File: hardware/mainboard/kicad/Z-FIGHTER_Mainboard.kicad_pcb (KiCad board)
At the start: 2 copper layers, 100 x 150 mm, 55 parts, among them IC1 Z80SIO, J1 DB9_Male_MountingHoles, J2 DB9_Male_MountingHoles, J3 USB_B, J4 Conn_02x13_Odd_Even, J5 Conn_Parallel_User, J6 Conn_PATA, J7 Conn_02x04_Odd_Even, SW1 SW_Push, SW2 SW_DIP_x03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

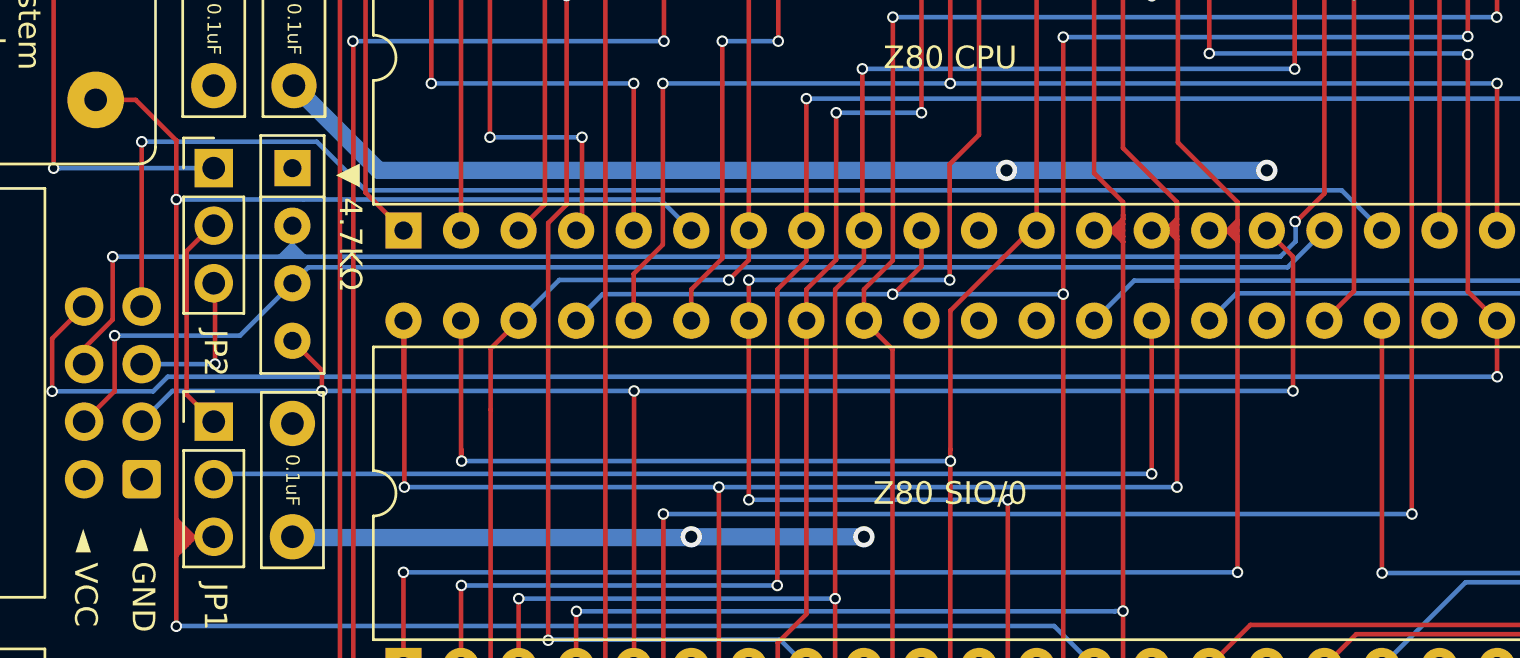
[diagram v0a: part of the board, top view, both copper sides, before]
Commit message: Added system clock to CPU control header
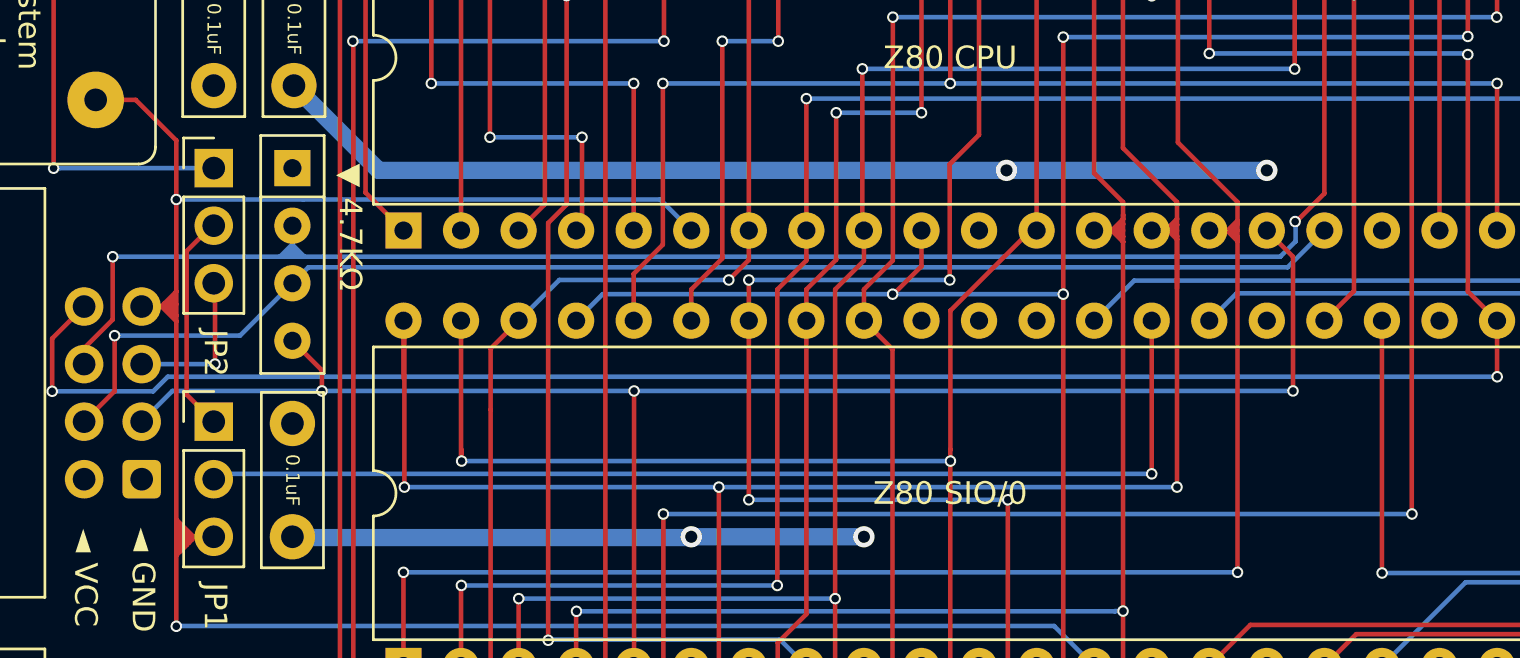
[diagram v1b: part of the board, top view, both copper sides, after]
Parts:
- moved G*** 1.12 mm to (143.8, 47.8)
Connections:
- J7 pad 7: HALT -> CLOCK
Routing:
- net HALT: track 63.6 -> 0.00 mm, vias 1 -> 0
- net CLOCK: track 122.2 -> 129.0 mm
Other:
- board text added: "Mainboard Rev. 2f"
- board text removed: "Mainboard Rev. 2e"

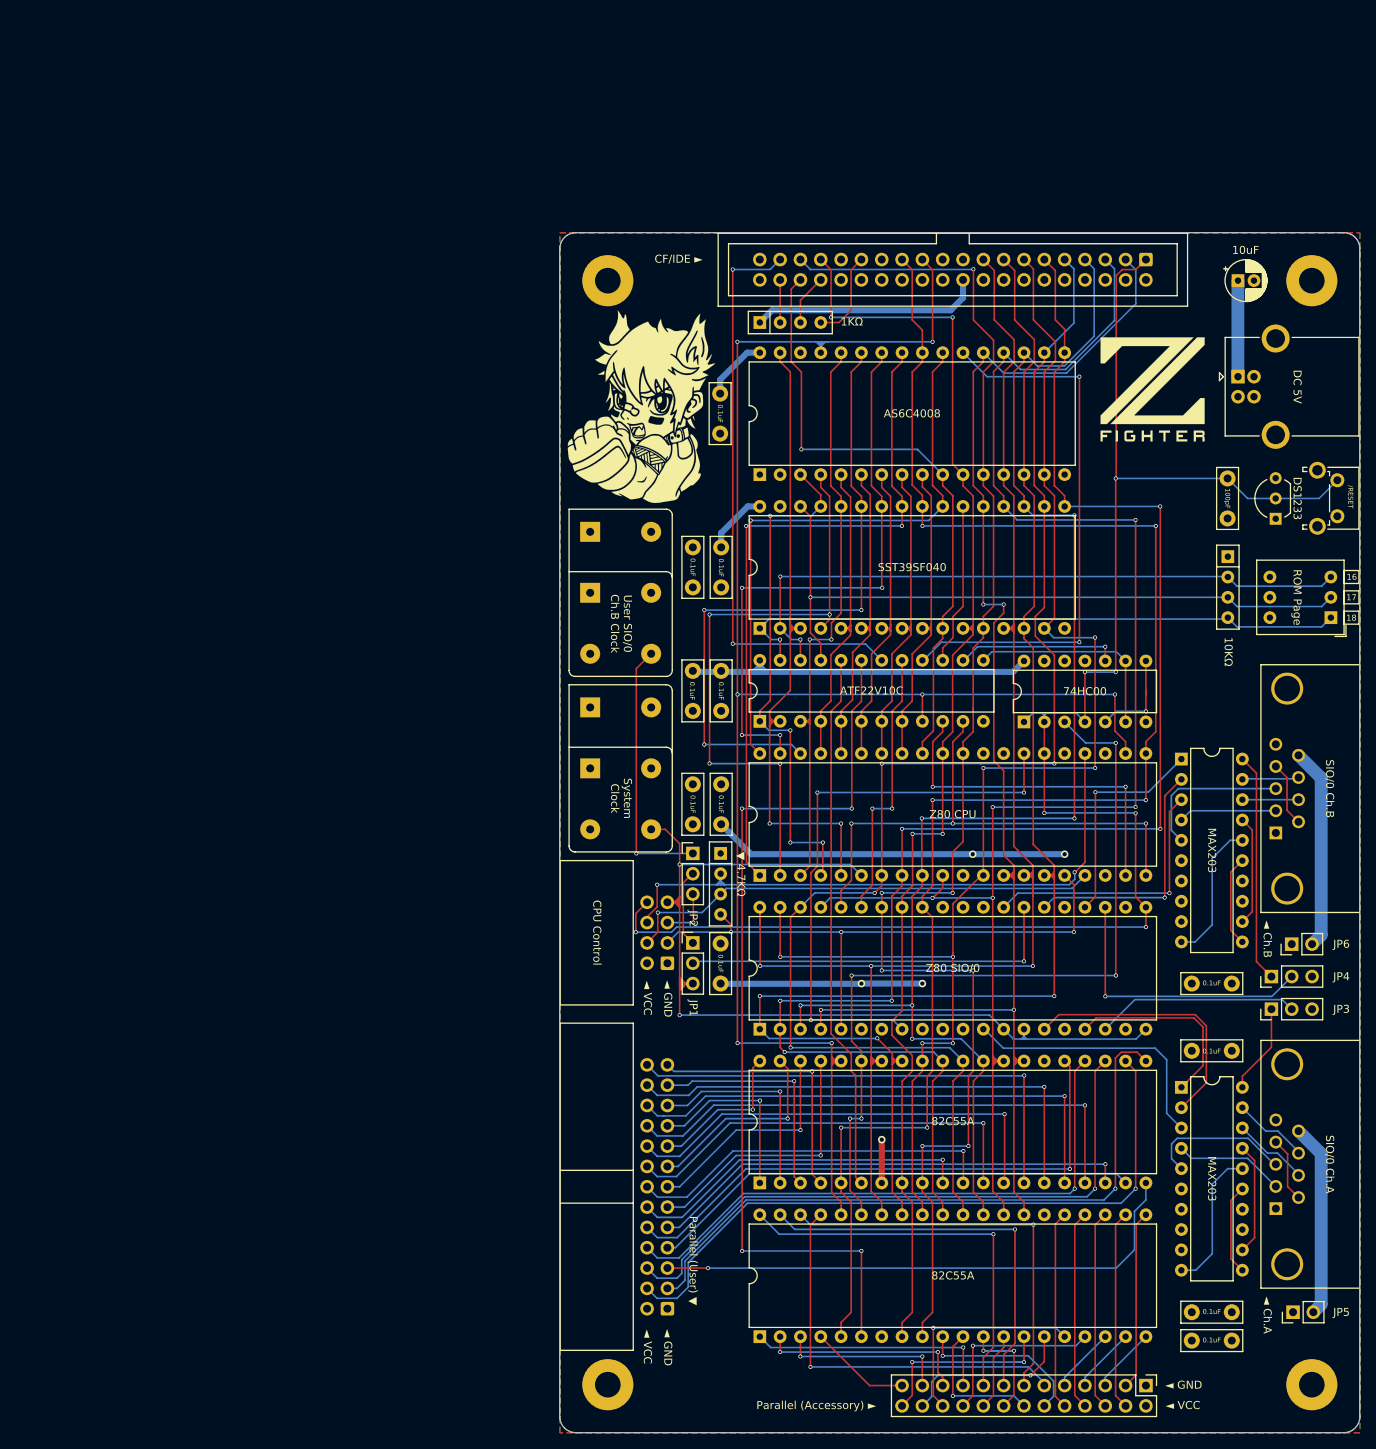
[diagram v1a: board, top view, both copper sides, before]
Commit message: Rounded corners
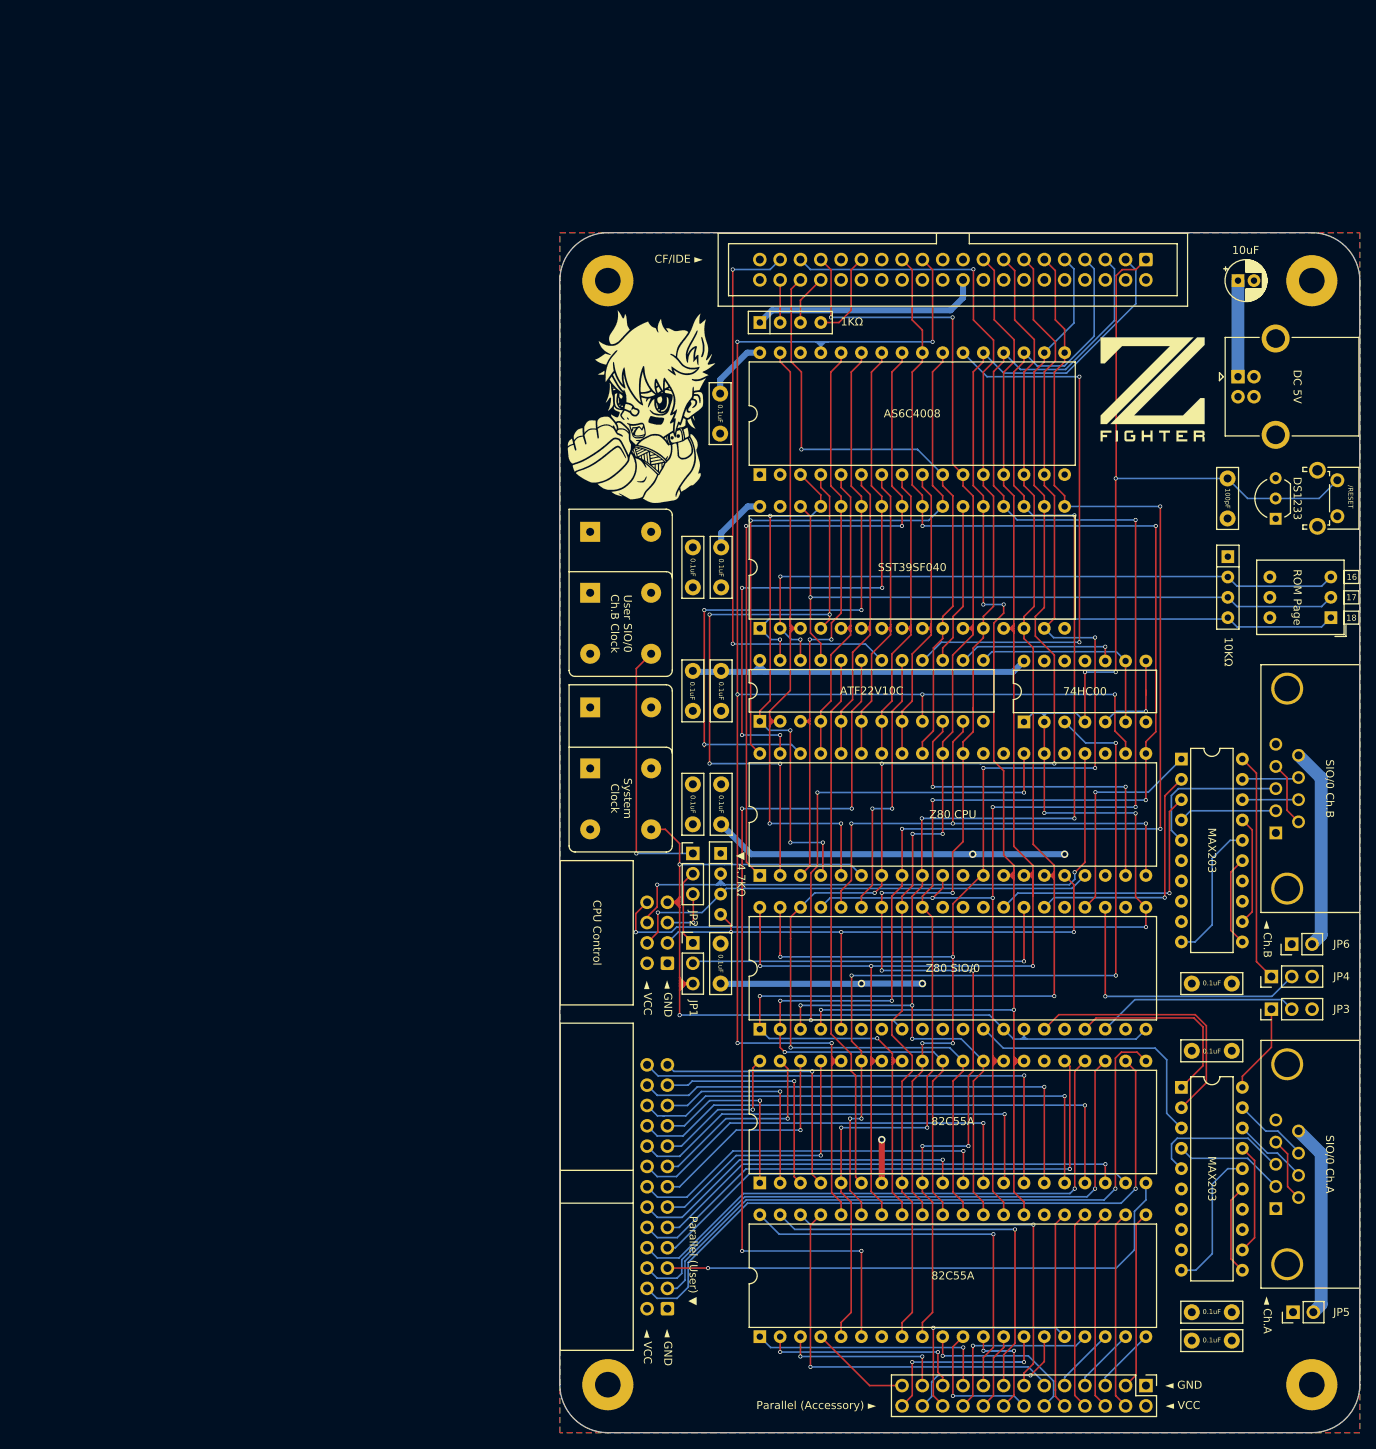
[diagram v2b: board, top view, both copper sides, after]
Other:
- outline, holes or cut-outs redrawn
- board text added: "Mainboard Rev. 2g"
- board text removed: "Mainboard Rev. 2f"

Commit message: Routing, plot, mainboard images
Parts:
- moved C10 73.1 mm to (79.0, 134.9)
- moved C12 73.1 mm to (79.0, 93.9)
- moved C13 73.1 mm to (84.0, 102.3)
- moved C14 73.1 mm to (16.6, 39.3)
- moved C2 73.1 mm to (83.5, 35.7)
- moved C3 73.1 mm to (16.6, 69.0)
- moved C4 73.1 mm to (20.0, 20.1)
- moved C5 73.1 mm to (79.0, 138.5)
- moved C9 73.1 mm to (16.6, 54.8)
- moved J1 73.1 mm to (89.5, 122.0)
- moved J2 73.1 mm to (89.5, 75.0)
- moved JP1 73.1 mm to (16.6, 88.8)
- moved JP2 73.1 mm to (16.6, 77.6)
- moved JP6 73.1 mm to (91.5, 88.9)
- moved Mount2 73.1 mm to (94.0, 6.00)
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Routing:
- net CLOCK: track 129.0 -> 112.6 mm
- net D0: track 183.3 -> 167.2 mm
- net D7: track 182.5 -> 170.8 mm
- net #WR: track 225.8 -> 217.3 mm
- net D1: track 185.7 -> 177.3 mm
- net A15: track 85.0 -> 77.0 mm
- net A7: track 41.6 -> 36.9 mm
- net #WAIT: track 79.1 -> 74.5 mm
- net D6: track 199.2 -> 194.5 mm
- net A6: track 41.4 -> 36.8 mm
- net A1: track 164.2 -> 160.8 mm
- net A5: track 40.0 -> 36.8 mm
- net A3: track 40.0 -> 36.8 mm
- net A4: track 39.9 -> 36.8 mm
- net VCC: track 173.3 -> 170.3 mm
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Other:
- net class Default removed
- net class Power removed
